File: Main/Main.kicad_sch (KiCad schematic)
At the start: 103 parts, among them J1 USB_B_Micro, J2 XT60, J3 Conn_01x03, J4 Conn_01x03, J5 Conn_01x03, J6 Conn_01x03, J7 MSD-4-A, J9 Conn_01x03, SW1 SW_Push, SW2 SW_Push, U1 RP2350A-QFN60, U10 LM75B, U11 MCS1802GS-50-Z, U12 MCS1802GS-50-Z, U13 MCS1802GS-50-Z, U14 TPS2121RUXR, U15 AP62150WU, U2 W25Q128JVS, U3 AMS1117-3.3, U4 MMC5983MA, U5 ICM-42688-P, U6 INA226, U7 KX134-1211, U8 MS5611-01BA, U9 MCS1802GS-50-Z, Y1 ABM8-272-T3

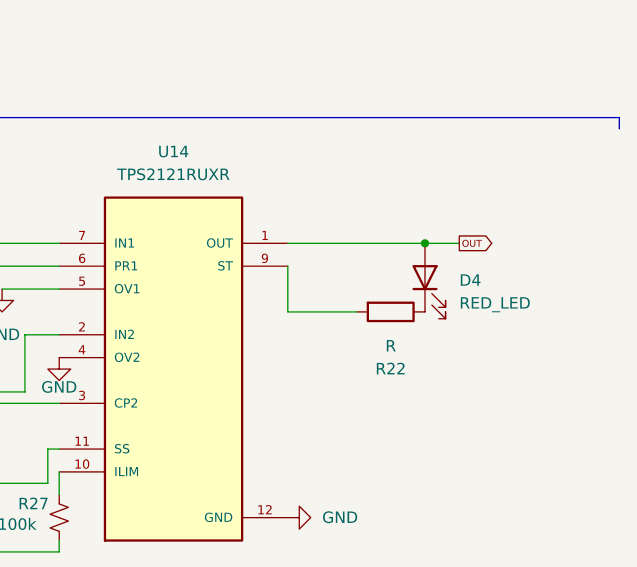
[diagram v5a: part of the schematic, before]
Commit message: updated power circuit layout
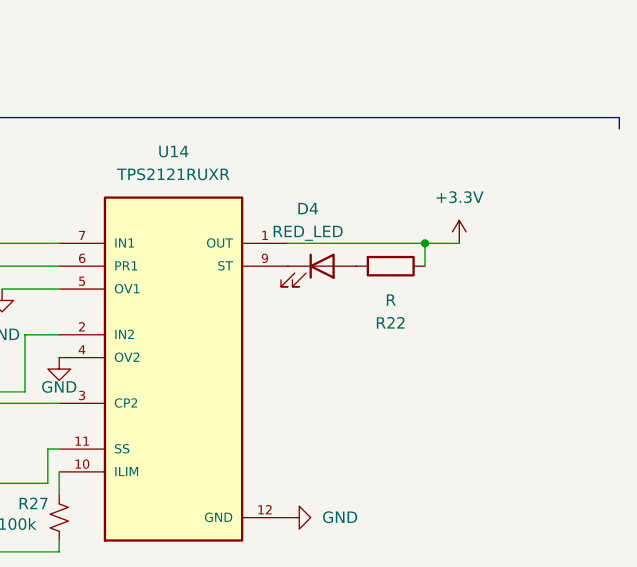
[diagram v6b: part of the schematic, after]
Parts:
- U14: footprint Package_DFN_QFN:Texas_VQFN-HR-12_2x2.5mm_P0.5mm_ThermalVias -> Package_DFN_QFN:Texas_VQFN-HR-12_2x2.5mm_P0.5mm
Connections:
- net +3.3V: now also R22.1, U14.1 (OUT), U14.8 (OUT)
- net 3.3v_Batt: no longer U14.2_1 (IN2)
- net 3.3v_usb: no longer U14.7_1 (IN1)
- net at D4.1 (K): now also U14.9 (ST); no longer R22.1
- net at R22.2: now also D4.2 (A); no longer U14.9 (ST)
- removed net OUT: D4.2 (A), U14.1 (OUT), U14.1_1 (OUT), U14.8 (OUT), U14.8_1 (OUT)
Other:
- moved on the sheet: D4, R22
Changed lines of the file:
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@@
 	)
 	(junction
+		(at 560.07 181.61)
+		(diameter 0)
+		(color 0 0 0 0)
+	)
+	(junction
 		(at 490.22 186.69)
 		(diameter 0)
@@
 	)
 	(junction
-		(at 560.07 181.61)
-		(diameter 0)
-		(color 0 0 0 0)
-	)
-	(junction
 		(at 234.95 187.96)
 		(diameter 0)
@@
 	(wire
 		(pts
-			(xy 563.88 181.61) (xy 560.07 181.61)
+			(xy 544.83 181.61) (xy 560.07 181.61)
 		)
 		(stroke
@@
 	(wire
 		(pts
-			(xy 544.83 189.23) (xy 544.83 184.15)
-		)
-		(stroke
-			(width 0)
-			(type default)
-		)
-	)
-	(wire
-		(pts
 			(xy 481.33 139.7) (xy 463.55 139.7)
 		)
@@
 	(wire
 		(pts
-			(xy 560.07 181.61) (xy 544.83 181.61)
-		)
-		(stroke
-			(width 0)
-			(type default)
-		)
-	)
-	(wire
-		(pts
 			(xy 515.62 191.77) (xy 519.43 191.77)
 		)
@@
 	(wire
 		(pts
+			(xy 560.07 181.61) (xy 560.07 184.15)
+		)
+		(stroke
+			(width 0)
+			(type default)
+		)
+	)
+	(wire
+		(pts
 			(xy 354.33 62.23) (xy 364.49 62.23)
 		)
@@
 	(wire
 		(pts
-			(xy 552.45 189.23) (xy 544.83 189.23)
-		)
-		(stroke
-			(width 0)
-			(type default)
-		)
-	)
-	(wire
-		(pts
 			(xy 156.21 276.86) (xy 166.37 276.86)
 		)
@@
 	(wire
 		(pts
+			(xy 560.07 181.61) (xy 563.88 181.61)
+		)
+		(stroke
+			(width 0)
+			(type default)
+		)
+	)
+	(wire
+		(pts
 			(xy 488.95 46.99) (xy 488.95 49.53)
 		)
@@
 		)
 	)
-	(global_label "OUT"
-		(shape output)
-		(at 563.88 181.61 0)
-		(fields_autoplaced yes)
-		(effects
-			(font
-				(size 0.762 0.762)
-			)
-			(justify left)
-		)
-		(property "Intersheetrefs" "${INTERSHEET_REFS}"
-			(at 567.8486 181.61 0)
-			(effects
-				(font
-					(size 1.27 1.27)
-				)
-				(justify left)
-				(hide yes)
-			)
-		)
-	)
 	(global_label "current -1"
 		(shape input)
@@
 	(symbol
 		(lib_id "Device:LED")
-		(at 560.07 185.42 90)
+		(at 548.64 184.15 0)
 		(unit 1)
 		(exclude_from_sim no)
@@
 		(fields_autoplaced yes)
 		(property "Reference" "D4"
-			(at 563.88 185.7374 90)
+			(at 547.0525 177.8 0)
 			(effects
 				(font
 					(size 1.27 1.27)
 				)
-				(justify right)
 			)
 		)
 		(property "Value" "RED_LED"
-			(at 563.88 188.2774 90)
+			(at 547.0525 180.34 0)
 			(effects
 				(font
 					(size 1.27 1.27)
 				)
-				(justify right)
 			)
 		)
 		(property "Footprint" "LED_SMD:LED_0805_2012Metric"
-			(at 560.07 185.42 0)
+			(at 548.64 184.15 0)
 			(effects
 				(font
@@
 		)
 		(property "Datasheet" "~"
-			(at 560.07 185.42 0)
+			(at 548.64 184.15 0)
 			(effects
 				(font
@@
 		)
 		(property "Description" "Light emitting diode"
-			(at 560.07 185.42 0)
+			(at 548.64 184.15 0)
 			(effects
 				(font
@@
 		)
 		(property "Sim.Pins" "1=K 2=A"
-			(at 560.07 185.42 0)
+			(at 548.64 184.15 0)
 			(effects
 				(font
@@
 		)
 		(property "JLCPCB Part #" ""
-			(at 560.07 185.42 0)
+			(at 548.64 184.15 0)
 			(effects
 				(font
@@
 		)
 		(property "Sim.Device" ""
-			(at 560.07 185.42 0)
+			(at 548.64 184.15 0)
 			(effects
 				(font
@@
 			)
 		)
-		(property "Footprint" "Package_DFN_QFN:Texas_VQFN-HR-12_2x2.5mm_P0.5mm_ThermalVias"
+		(property "Footprint" "Package_DFN_QFN:Texas_VQFN-HR-12_2x2.5mm_P0.5mm"
 			(at 532.13 196.85 0)
 			(effects
@@
 		(pin "9"
 		)
-		(pin "8_1"
-		)
 		(pin "8"
 		)
-		(pin "1_1"
-		)
 		(pin "1"
 		)
@@
 		(pin "4"
 		)
-		(pin "2_1"
-		)
 		(pin "2"
 		)
@@
 		(pin "6"
 		)
-		(pin "7_1"
-		)
 		(instances
 			(project "Main"
@@
 	(symbol
 		(lib_id "Device:R")
-		(at 556.26 189.23 270)
+		(at 556.26 184.15 270)
 		(unit 1)
 		(exclude_from_sim no)
@@
 		(fields_autoplaced yes)
 		(property "Reference" "R22"
-			(at 556.26 195.58 90)
+			(at 556.26 190.5 90)
 			(effects
 				(font
@@
 		)
 		(property "Value" "R"
-			(at 556.26 193.04 90)
+			(at 556.26 187.96 90)
 			(effects
 				(font
@@
 		)
 		(property "Footprint" "Resistor_SMD:R_0402_1005Metric"
-			(at 556.26 187.452 90)
+			(at 556.26 182.372 90)
 			(effects
 				(font
@@
 		)
 		(property "Datasheet" "~"
-			(at 556.26 189.23 0)
+			(at 556.26 184.15 0)
 			(effects
 				(font
@@
 		)
 		(property "Description" "Resistor"
-			(at 556.26 189.23 0)
+			(at 556.26 184.15 0)
 			(effects
 				(font
@@
 		)
 		(property "JLCPCB Part #" ""
-			(at 556.26 189.23 90)
+			(at 556.26 184.15 90)
 			(effects
 				(font
@@
 		)
 		(property "Sim.Device" ""
-			(at 556.26 189.23 90)
+			(at 556.26 184.15 90)
 			(effects
 				(font
@@
 					(unit 1)
 				)
+			)
+		)
+	)
+	(symbol
+		(lib_id "power:+3.3V")
+		(at 563.88 181.61 0)
+		(unit 1)
+		(exclude_from_sim no)
+		(in_bom yes)
+		(on_board yes)
+		(dnp no)
+		(fields_autoplaced yes)
+		(property "Reference" "#PWR083"
+			(at 563.88 185.42 0)
+			(effects
+				(font
+					(size 1.27 1.27)
+				)
+				(hide yes)
+			)
+		)
+		(property "Value" "+3.3V"
+			(at 563.88 176.53 0)
+			(effects
+				(font
+					(size 1.27 1.27)
+				)
+			)
+		)
+		(property "Footprint" ""
+			(at 563.88 181.61 0)
+			(effects
+				(font
+					(size 1.27 1.27)
+				)
+				(hide yes)
+			)
+		)
+		(property "Datasheet" ""
+			(at 563.88 181.61 0)
+			(effects
+				(font
+					(size 1.27 1.27)
+				)
+				(hide yes)
+			)
+		)
+		(property "Description" "Power symbol creates a global label with name \"+3.3V\""
+			(at 563.88 181.61 0)
+			(effects
+				(font
+					(size 1.27 1.27)
+				)
+				(hide yes)
+			)
+		)
+		(pin "1"
+		)
+		(instances
+			(project "Main"
+				(path "/6b66026e-3aa1-4d5a-a331-be21386153c7"
+					(reference "#PWR083")
+					(unit 1)
+				)

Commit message: Wiring Mostly Done
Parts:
- D2: value BLUE_LED -> YELLOW_LED
- R10, R22: value R -> 60
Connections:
- net ACCEL_INT1 is gone; now on net ACCEL_INT: U7.5 (INT1)
- net ACCEL_nCS is gone; now on net ACCEL_CS: U7.10 (nCS)
- net IO_VDD is gone; now on net +3.3V: C25.1, U7.3 (IO_VDD)
- net SCLK is gone; now on net SPI_SCK: U8.8 (SCLK)
- net SDI is gone; now on net SPI_SDI: U8.7 (SDI/SDA)
- net SDO is gone; now on net SPI_SDO: U8.6 (SDO)
- net SPI_SD0 is gone; now on net SPI_SDO: U4.5 (SPI_SDO), U5.1 (AP_SDO/AP_AD0), U7.1 (SDO/ADDR)
- net VDD is gone; now on net +3.3V: C26.2, U7.7 (VDD)
- net ICM_CS: now also U1.17 (GPIO13)
- net INT2/DRDY: now also U1.27 (GPIO16)
- net MMC_CS: now also U1.18 (GPIO14)
- net MS5611_CS: now also U1.16 (GPIO12)
- net PWM1: now also U1.31 (GPIO19)
- net PWM2: now also U1.34 (GPIO22)
- net PWM3: now also U1.36 (GPIO24)
- net PWM4: now also U1.35 (GPIO23)
- net SD_CD: now also U1.7 (GPIO4)
- net SD_ChipSelect: now also U1.3 (GPIO1)
- net SPI_SCK: now also U1.14 (GPIO10)
- net SPI_SCLK2: now also U1.4 (GPIO2)
- net SPI_SDI: now also U1.15 (GPIO11)
- net SPI_SDI2: now also U1.5 (GPIO3)
- net SPI_SDO2: now also U1.2 (GPIO0)
- net MMC_INT: now reaches U4.15 (INT)
- net MMC_INT: now also U1.29 (GPIO18)
- net SPI_SDO: now reaches U1.12 (GPIO8)
- net ACCEL_CS: now reaches U1.19 (GPIO15)
- net ACCEL_INT: now reaches U1.28 (GPIO17)
- net ACCEL_INT2: no longer names the net of U7.6 (INT2)
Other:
- note added: "INT HIGH when reading available"
- note added: "SPI_1: ICM (IMU) KX-134(HIGH G-Accel) MMC (Magnetometer) MS5611 (Barometer)"
- moved on the sheet: U8

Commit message: PART NUMBERSSSSS
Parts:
- C1, C2, C3, C4: LCSC Part Number (none) -> C318563
- C10, C11, C12, C13, C14, C15, C19, C24, C25, C26, C27, C28, C29, C30, C31, C32, C33, C34, C38, C40, C5, C6, C7, C8, C9: LCSC Part Number (none) -> C1525
- C16, C17: LCSC Part Number (none) -> C1548
- C18, C20, C21, C23, C37, C39: LCSC Part Number (none) -> C1713
- C22, C35: LCSC Part Number (none) -> C1712
- C41: LCSC Part Number (none) -> C45783
- D1, D4: LCSC Part Number (none) -> C2295
- D2: LCSC Part Number (none) -> C2296
- D3: LCSC Part Number (none) -> C2297
- R1: LCSC Part Number (none) -> C25105
- R10, R22: value 60 -> 100; LCSC Part Number (none) -> C25076
- R11, R12: value R -> 100; LCSC Part Number (none) -> C25076
- R14, R15, R16, R17, R18, R21, R9: LCSC Part Number (none) -> C25531
- R19, R20: LCSC Part Number (none) -> C25553
- R2, R3: LCSC Part Number (none) -> C25092
- R23, R4, R5, R6: LCSC Part Number (none) -> C11702
- R24, R25, R26, R27: LCSC Part Number (none) -> C25741
- R7, R8: LCSC Part Number (none) -> C25900
- U1: LCSC Part Number (none) -> C42411118
- U10: LCSC Part Number (none) -> C34565
- U11, U12, U13, U9: LCSC Part Number (none) -> C3684509
- U14: LCSC Part Number (none) -> C485916
- U15: LCSC Part Number (none) -> C3194237
- U2: LCSC Part Number (none) -> C97521
- U3: LCSC Part Number (none) -> C6186
- U4: LCSC Part Number (none) -> C404329
- U5: LCSC Part Number (none) -> C48586483
- U6: LCSC Part Number (none) -> C49851
- U7: LCSC Part Number (none) -> C2157908
- U8: LCSC Part Number (none) -> C15639
- Y1: LCSC Part Number (none) -> C20625731
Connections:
- net LED1: now also U1.37 (GPIO25)
- net LED2: now also U1.8 (GPIO5)
